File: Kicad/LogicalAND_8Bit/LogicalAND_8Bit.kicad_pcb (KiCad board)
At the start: 2 copper layers, 39.3 x 66.3 mm, 65 parts, among them J1 Conn_01x26_Pin, Q1 NPN, Q10 NPN, Q11 NPN, Q12 NPN, Q13 NPN, Q14 NPN, Q15 NPN, Q16 NPN, Q17 NPN, Q18 NPN, Q19 NPN, Q2 NPN, Q20 NPN, Q21 NPN, Q22 NPN, Q23 NPN, Q24 NPN, Q3 NPN, Q4 NPN, Q5 NPN, Q6 NPN, Q7 NPN, Q8 NPN, Q9 NPN

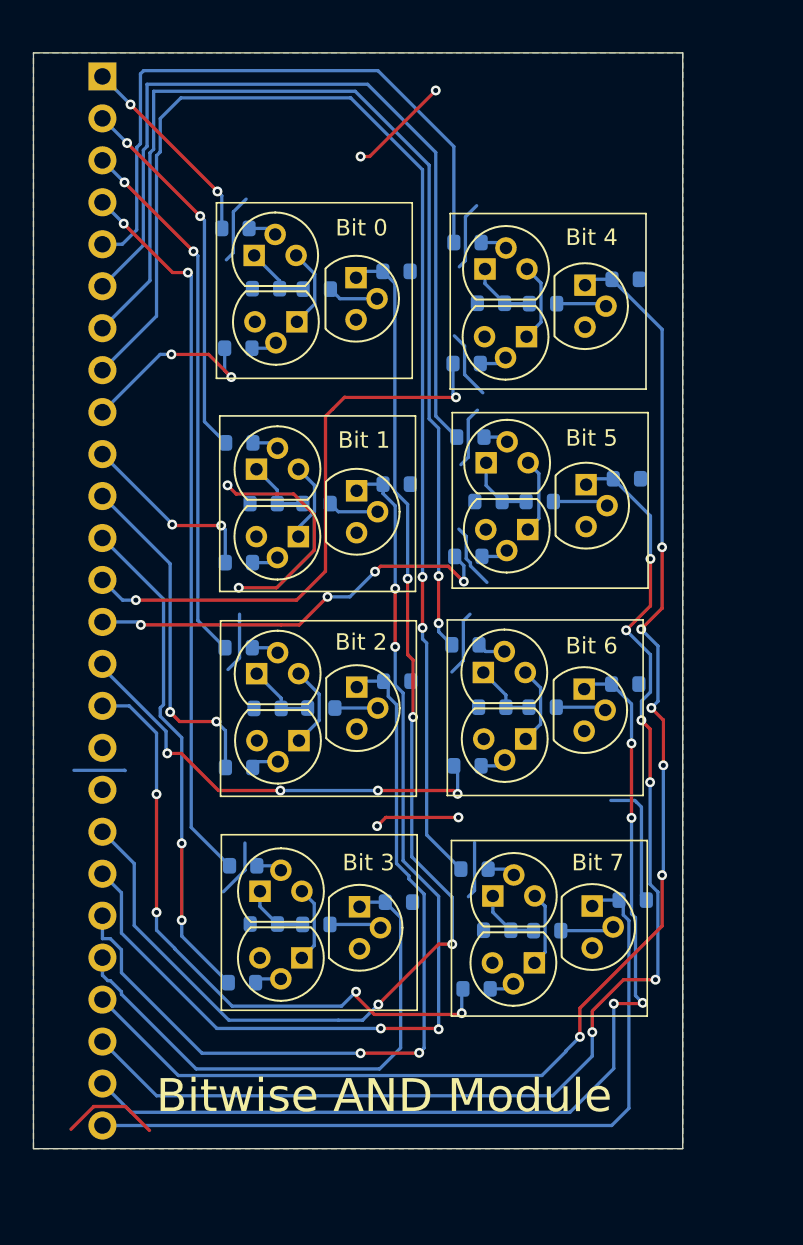
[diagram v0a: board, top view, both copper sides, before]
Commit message: Finished the XOR module and added silk screens to OR, AND, and XOR
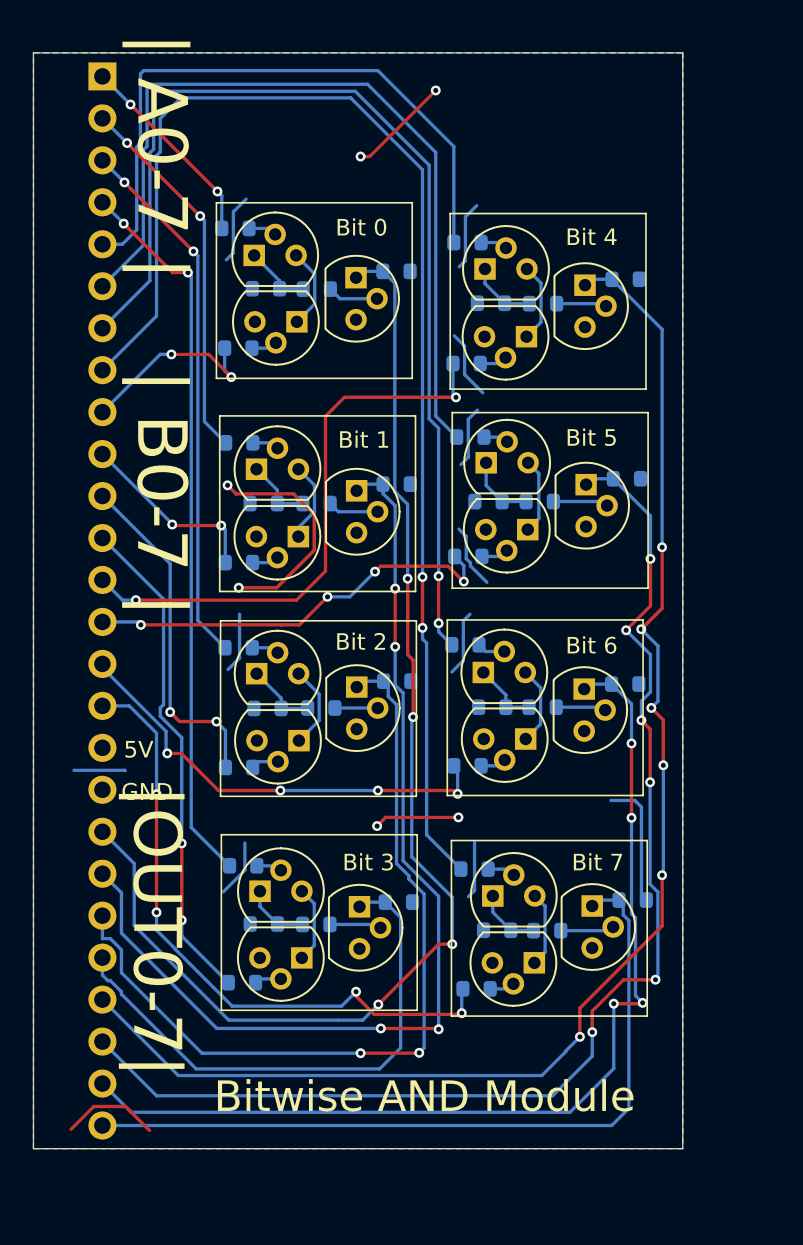
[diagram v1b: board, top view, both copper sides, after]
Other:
- board text added: "5V"
- board text added: "GND"
- board text added: "| A0-7 |"
- board text added: "| B0-7 |"
- board text added: "|OUT0-7|"
